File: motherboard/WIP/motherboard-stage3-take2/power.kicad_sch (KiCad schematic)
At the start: 9 parts, among them J3 Power, J5 Reset, U10 BA05CCOT, U11 MAX708

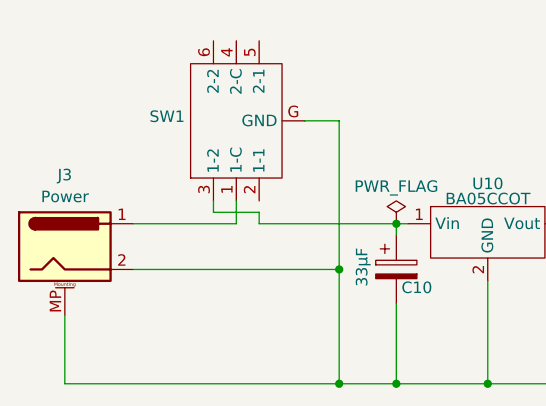
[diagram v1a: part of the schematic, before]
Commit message: Updated stage 2 and stage 3, and started on a cf addon
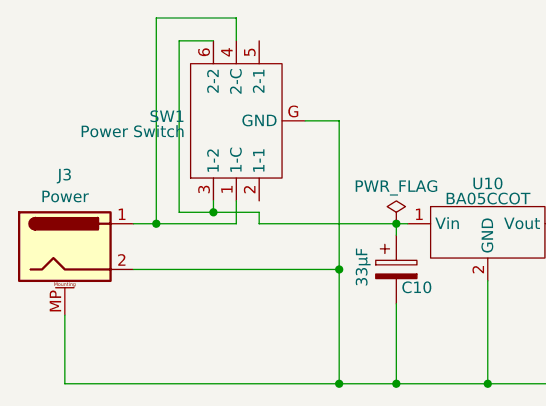
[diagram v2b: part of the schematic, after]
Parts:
- SW1: value ~ -> Power Switch
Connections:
- net at C10.1, SW1.3 (1-2), U10.1 (Vin): now also SW1.6 (2-2)
- net at J3.1, SW1.1 (1-C): now also SW1.4 (2-C)
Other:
- company: (none) -> Eric Lind
- title: (none) -> MicroLind - PSU & Reset
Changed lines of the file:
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@@
 	(generator_version "8.0")
 	(paper "A4")
+	(title_block
+		(title "MicroLind - PSU & Reset")
+		(date "2025-03-03")
+		(rev "C0")
+		(company "Eric Lind")
+	)
 	(junction
 		(at 133.35 144.78)
@@
 	)
 	(junction
+		(at 96.52 127)
+		(diameter 0)
+		(color 0 0 0 0)
+	)
+	(junction
 		(at 153.67 127)
 		(diameter 0)
@@
 	(junction
 		(at 116.84 144.78)
+		(diameter 0)
+		(color 0 0 0 0)
+	)
+	(junction
+		(at 102.87 125.73)
 		(diameter 0)
 		(color 0 0 0 0)
@@
 	(wire
 		(pts
+			(xy 96.52 127) (xy 105.41 127)
+		)
+		(stroke
+			(width 0)
+			(type default)
+		)
+	)
+	(wire
+		(pts
 			(xy 198.12 127) (xy 198.12 128.27)
 		)
@@
 	(wire
 		(pts
+			(xy 96.52 104.14) (xy 105.41 104.14)
+		)
+		(stroke
+			(width 0)
+			(type default)
+		)
+	)
+	(wire
+		(pts
+			(xy 99.06 125.73) (xy 99.06 106.68)
+		)
+		(stroke
+			(width 0)
+			(type default)
+		)
+	)
+	(wire
+		(pts
 			(xy 133.35 144.78) (xy 146.05 144.78)
 		)
@@
 	(wire
 		(pts
+			(xy 102.87 125.73) (xy 99.06 125.73)
+		)
+		(stroke
+			(width 0)
+			(type default)
+		)
+	)
+	(wire
+		(pts
 			(xy 198.12 143.51) (xy 198.12 144.78)
 		)
@@
 	(wire
 		(pts
+			(xy 105.41 104.14) (xy 105.41 106.68)
+		)
+		(stroke
+			(width 0)
+			(type default)
+		)
+	)
+	(wire
+		(pts
 			(xy 153.67 127) (xy 153.67 128.27)
 		)
@@
 	(wire
 		(pts
-			(xy 93.98 127) (xy 105.41 127)
+			(xy 93.98 127) (xy 96.52 127)
 		)
 		(stroke
@@
 	(wire
 		(pts
+			(xy 99.06 106.68) (xy 102.87 106.68)
+		)
+		(stroke
+			(width 0)
+			(type default)
+		)
+	)
+	(wire
+		(pts
 			(xy 160.02 127) (xy 160.02 124.46)
+		)
+		(stroke
+			(width 0)
+			(type default)
+		)
+	)
+	(wire
+		(pts
+			(xy 96.52 127) (xy 96.52 104.14)
 		)
 		(stroke
@@
 			)
 		)
-		(property "Value" "~"
+		(property "Value" "Power Switch"
 			(at 99.695 116.7822 90)
 			(effects

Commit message: Updates to a lot!
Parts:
- added J18: +12v, Connector_PinHeader_2.54mm:PinHeader_1x01_P2.54mm_Vertical, symbol Connector_Generic:Conn_01x01
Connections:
- new net +12V: J18.1 (Pin_1)
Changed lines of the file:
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@@
+	(wire
+		(pts
+			(xy 191.77 113.03) (xy 189.23 113.03)
+		)
+		(stroke
+			(width 0)
+			(type default)
+		)
+	)
 	(wire
 		(pts
@@
 		(pts
 			(xy 146.05 144.78) (xy 153.67 144.78)
+		)
+		(stroke
+			(width 0)
+			(type default)
+		)
+	)
+	(wire
+		(pts
+			(xy 189.23 113.03) (xy 189.23 110.49)
 		)
 		(stroke
@@
 	)
 	(symbol
+		(lib_id "Connector_Generic:Conn_01x01")
+		(at 196.85 113.03 0)
+		(unit 1)
+		(exclude_from_sim no)
+		(in_bom yes)
+		(on_board yes)
+		(dnp no)
+		(fields_autoplaced yes)
+		(property "Reference" "J18"
+			(at 198.882 111.8178 0)
+			(effects
+				(font
+					(size 1.27 1.27)
+				)
+				(justify left)
+			)
+		)
+		(property "Value" "+12v"
+			(at 198.882 114.2421 0)
+			(effects
+				(font
+					(size 1.27 1.27)
+				)
+				(justify left)
+			)
+		)
+		(property "Footprint" "Connector_PinHeader_2.54mm:PinHeader_1x01_P2.54mm_Vertical"
+			(at 196.85 113.03 0)
+			(effects
+				(font
+					(size 1.27 1.27)
+				)
+				(hide yes)
+			)
+		)
+		(property "Datasheet" "~"
+			(at 196.85 113.03 0)
+			(effects
+				(font
+					(size 1.27 1.27)
+				)
+				(hide yes)
+			)
+		)
+		(property "Description" "Generic connector, single row, 01x01, script generated (kicad-library-utils/schlib/autogen/connector/)"
+			(at 196.85 113.03 0)
+			(effects
+				(font
+					(size 1.27 1.27)
+				)
+				(hide yes)
+			)
+		)
+		(pin "1"
+		)
+		(instances
+			(project ""
+				(path "/4cf1c087-5c32-4958-ab30-5e92afc4ef4b/2674a088-a7e1-45c5-a464-4e213ad1e901"
+					(reference "J18")
+					(unit 1)
+				)
+			)
+		)
+	)
+	(symbol
 		(lib_id "Switch:SW_Push")
 		(at 172.72 139.7 0)
@@
 					(unit 1)
 				)
+			)
+		)
+	)
+	(symbol
+		(lib_id "power:+12V")
+		(at 189.23 110.49 0)
+		(unit 1)
+		(exclude_from_sim no)
+		(in_bom yes)
+		(on_board yes)
+		(dnp no)
+		(fields_autoplaced yes)
+		(property "Reference" "#PWR0125"
+			(at 189.23 114.3 0)
+			(effects
+				(font
+					(size 1.27 1.27)
+				)
+				(hide yes)
+			)
+		)
+		(property "Value" "+12V"
+			(at 189.23 106.3569 0)
+			(effects
+				(font
+					(size 1.27 1.27)
+				)
+			)
+		)
+		(property "Footprint" ""
+			(at 189.23 110.49 0)
+			(effects
+				(font
+					(size 1.27 1.27)
+				)
+				(hide yes)
+			)
+		)
+		(property "Datasheet" ""
+			(at 189.23 110.49 0)
+			(effects
+				(font
+					(size 1.27 1.27)
+				)
+				(hide yes)
+			)
+		)
+		(property "Description" "Power symbol creates a global label with name \"+12V\""
+			(at 189.23 110.49 0)
+			(effects
+				(font
+					(size 1.27 1.27)
+				)
+				(hide yes)
+			)
+		)
+		(pin "1"
+		)
+		(instances
+			(project ""
+				(path "/4cf1c087-5c32-4958-ab30-5e92afc4ef4b/2674a088-a7e1-45c5-a464-4e213ad1e901"
+					(reference "#PWR0125")
+					(unit 1)
+				)

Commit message: Updates
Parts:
- renumbered J18 to J16, J3 to P7

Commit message: Updated stage 3
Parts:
- removed U10: BA05CCOT, PCM_Package_TO_SOT_THT_AKL:TO-220-3_Horizontal_TabDown, symbol motherboard:BA05CC0T
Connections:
- net VCC: now also C10.1, SW1.3 (1-2), SW1.6 (2-2)
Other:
- moved on the sheet: C11, C12
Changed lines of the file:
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@@
-	)
-	(junction
-		(at 133.35 144.78)
-		(diameter 0)
-		(color 0 0 0 0)
 	)
 	(junction
@@
 	(wire
 		(pts
-			(xy 133.35 144.78) (xy 146.05 144.78)
-		)
-		(stroke
-			(width 0)
-			(type default)
-		)
-	)
-	(wire
-		(pts
 			(xy 160.02 127) (xy 179.07 127)
 		)
@@
 	(wire
 		(pts
-			(xy 123.19 127) (xy 124.46 127)
-		)
-		(stroke
-			(width 0)
-			(type default)
-		)
-	)
-	(wire
-		(pts
-			(xy 133.35 133.35) (xy 133.35 144.78)
+			(xy 123.19 127) (xy 146.05 127)
 		)
 		(stroke
@@
 	(wire
 		(pts
-			(xy 153.67 127) (xy 153.67 128.27)
+			(xy 153.67 127) (xy 153.67 133.35)
 		)
 		(stroke
@@
 	(wire
 		(pts
-			(xy 146.05 128.27) (xy 146.05 127)
+			(xy 146.05 133.35) (xy 146.05 127)
 		)
 		(stroke
@@
 	(wire
 		(pts
-			(xy 123.19 144.78) (xy 133.35 144.78)
-		)
-		(stroke
-			(width 0)
-			(type default)
-		)
-	)
-	(wire
-		(pts
-			(xy 153.67 135.89) (xy 153.67 144.78)
+			(xy 123.19 144.78) (xy 146.05 144.78)
+		)
+		(stroke
+			(width 0)
+			(type default)
+		)
+	)
+	(wire
+		(pts
+			(xy 153.67 140.97) (xy 153.67 144.78)
 		)
 		(stroke
@@
 	(wire
 		(pts
-			(xy 142.24 127) (xy 146.05 127)
-		)
-		(stroke
-			(width 0)
-			(type default)
-		)
-	)
-	(wire
-		(pts
-			(xy 146.05 135.89) (xy 146.05 144.78)
+			(xy 146.05 140.97) (xy 146.05 144.78)
 		)
 		(stroke
@@
 	)
 	(symbol
-		(lib_id "motherboard:BA05CC0T")
-		(at 130.81 133.35 0)
-		(unit 1)
-		(exclude_from_sim no)
-		(in_bom yes)
-		(on_board yes)
-		(dnp no)
-		(fields_autoplaced yes)
-		(property "Reference" "U10"
-			(at 133.35 122.5635 0)
-			(effects
-				(font
-					(size 1.27 1.27)
-				)
-			)
-		)
-		(property "Value" "BA05CCOT"
-			(at 133.35 124.2449 0)
-			(effects
-				(font
-					(size 1.27 1.27)
-				)
-			)
-		)
-		(property "Footprint" "PCM_Package_TO_SOT_THT_AKL:TO-220-3_Horizontal_TabDown"
-			(at 130.81 133.35 0)
-			(effects
-				(font
-					(size 1.27 1.27)
-				)
-				(hide yes)
-			)
-		)
-		(property "Datasheet" ""
-			(at 130.81 133.35 0)
-			(effects
-				(font
-					(size 1.27 1.27)
-				)
-				(hide yes)
-			)
-		)
-		(property "Description" ""
-			(at 130.81 133.35 0)
-			(effects
-				(font
-					(size 1.27 1.27)
-				)
-				(hide yes)
-			)
-		)
-		(pin "3"
-		)
-		(pin "2"
-		)
-		(pin "1"
-		)
-		(instances
-			(project "motherboard"
-				(path "/4cf1c087-5c32-4958-ab30-5e92afc4ef4b/2674a088-a7e1-45c5-a464-4e213ad1e901"
-					(reference "U10")
-					(unit 1)
-				)
-			)
-		)
-	)
-	(symbol
 		(lib_id "Device:C_Polarized")
-		(at 146.05 132.08 0)
+		(at 146.05 137.16 0)
 		(unit 1)
 		(exclude_from_sim no)
@@
 		(dnp no)
 		(property "Reference" "C11"
-			(at 145.796 125.222 0)
+			(at 146.05 124.968 0)
 			(effects
 				(font
@@
 		)
 		(property "Value" "100µF"
-			(at 141.986 131.572 90)
+			(at 141.986 136.652 90)
 			(effects
 				(font
@@
 		)
 		(property "Footprint" "Capacitor_THT:CP_Radial_D6.3mm_P2.50mm"
-			(at 147.0152 135.89 0)
+			(at 147.0152 140.97 0)
 			(effects
 				(font
@@
 		)
 		(property "Datasheet" "~"
-			(at 146.05 132.08 0)
+			(at 146.05 137.16 0)
 			(effects
 				(font
@@
 		)
 		(property "Description" "Polarized capacitor"
-			(at 146.05 132.08 0)
+			(at 146.05 137.16 0)
 			(effects
 				(font
@@
 	(symbol
 		(lib_id "Device:C_Polarized")
-		(at 153.67 132.08 0)
+		(at 153.67 137.16 0)
 		(unit 1)
 		(exclude_from_sim no)
@@
 		)
 		(property "Value" "10µF"
-			(at 149.606 131.572 90)
+			(at 149.606 136.652 90)
 			(effects
 				(font
@@
 		)
 		(property "Footprint" "Capacitor_THT:CP_Radial_D4.0mm_P2.00mm"
-			(at 154.6352 135.89 0)
+			(at 154.6352 140.97 0)
 			(effects
 				(font
@@
 		)
 		(property "Datasheet" "~"
-			(at 153.67 132.08 0)
+			(at 153.67 137.16 0)
 			(effects
 				(font
@@
 		)
 		(property "Description" "Polarized capacitor"
-			(at 153.67 132.08 0)
-			(effects
-				(font
+			(at 153.67 137.16 0)
+			(effects
+				(font
